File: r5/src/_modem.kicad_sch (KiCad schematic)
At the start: 54 parts, among them J1 , J12 U_FL-R-SMT-1_10_, J13 JAE_SIM_Card_SF72S006, J17 DNP, J2 , J3 , J4 , J5 , J6 , J7 , J8 , J9 , Q11 NX3008NBKW, Q5 NX3008NBKW, Q6 NX3008NBKW, Q7 NX3008NBKW, Q8 NX3008NBKW, Q9 NX3008NBKW, T10 , T11 , T8 , T9 , U7 Sierra_Wireless_RC7620, U8 ESD7004

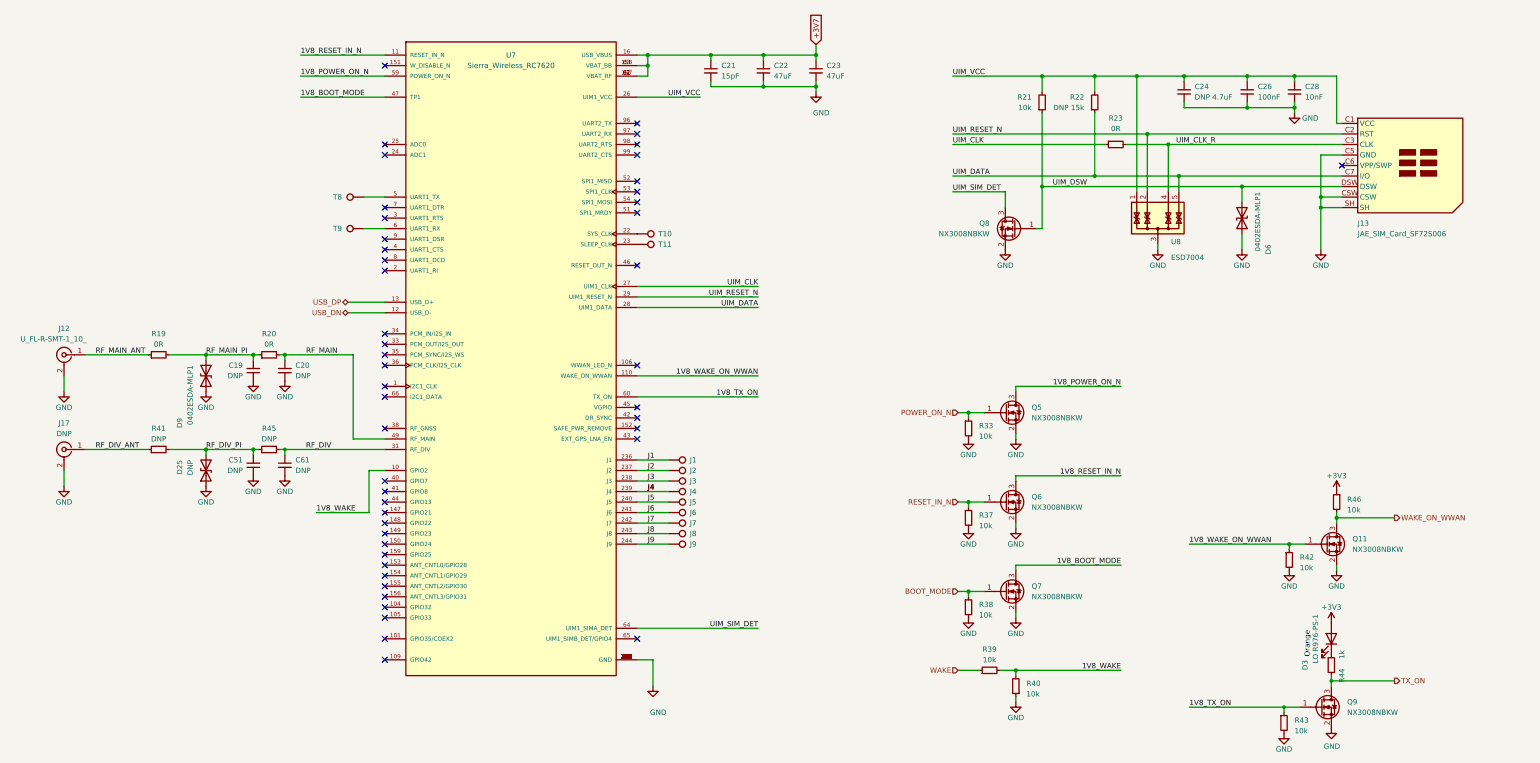
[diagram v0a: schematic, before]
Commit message: Updates to +/-15V supply. Additional output capacitance. Change to smaller inductor packages. Add 0R links to permit isolation of output. Mods to compensation network. Set feedback resistors to datasheet values.
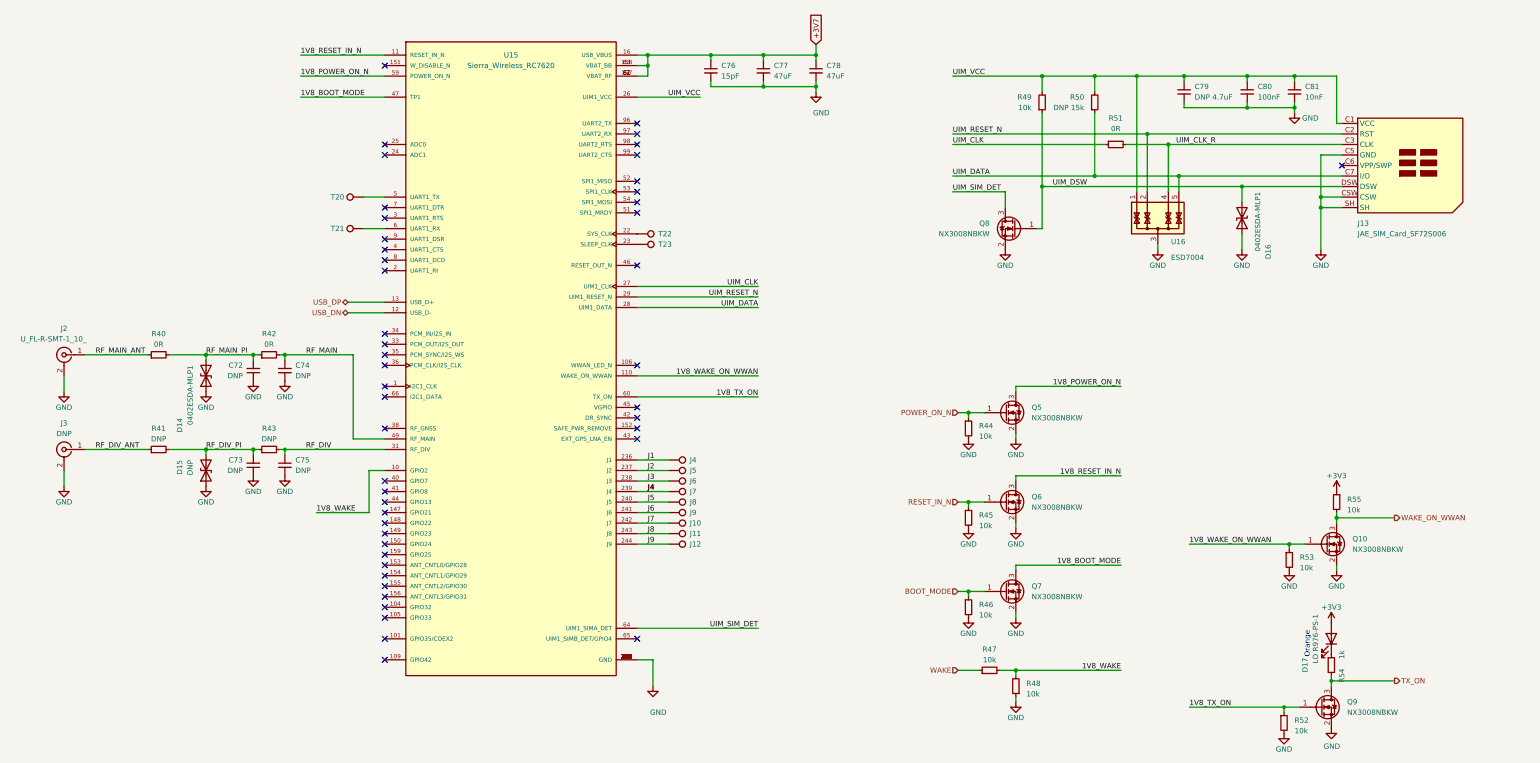
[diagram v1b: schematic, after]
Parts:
- renumbered C19 to C72, C51 to C73, C20 to C74, C61 to C75, C21 to C76, C22 to C77, C23 to C78, C24 to C79, C26 to C80, C28 to C81, D9 to D14, D25 to D15, D6 to D16, D3 to D17, J7 to J10, J8 to J11, J9 to J12, J12 to J2, J17 to J3, J1 to J4, J2 to J5, J3 to J6, J4 to J7, J5 to J8, J6 to J9, Q11 to Q10, R19 to R40, R20 to R42, R45 to R43, R33 to R44, R37 to R45, R38 to R46, R39 to R47, R40 to R48, R21 to R49, R22 to R50, R23 to R51, R43 to R52, R42 to R53, R44 to R54, R46 to R55, T8 to T20, T9 to T21, T10 to T22, T11 to T23, U7 to U15, U8 to U16

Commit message: Fix broken component annotation by importing back from PCB and fixing duplicates.
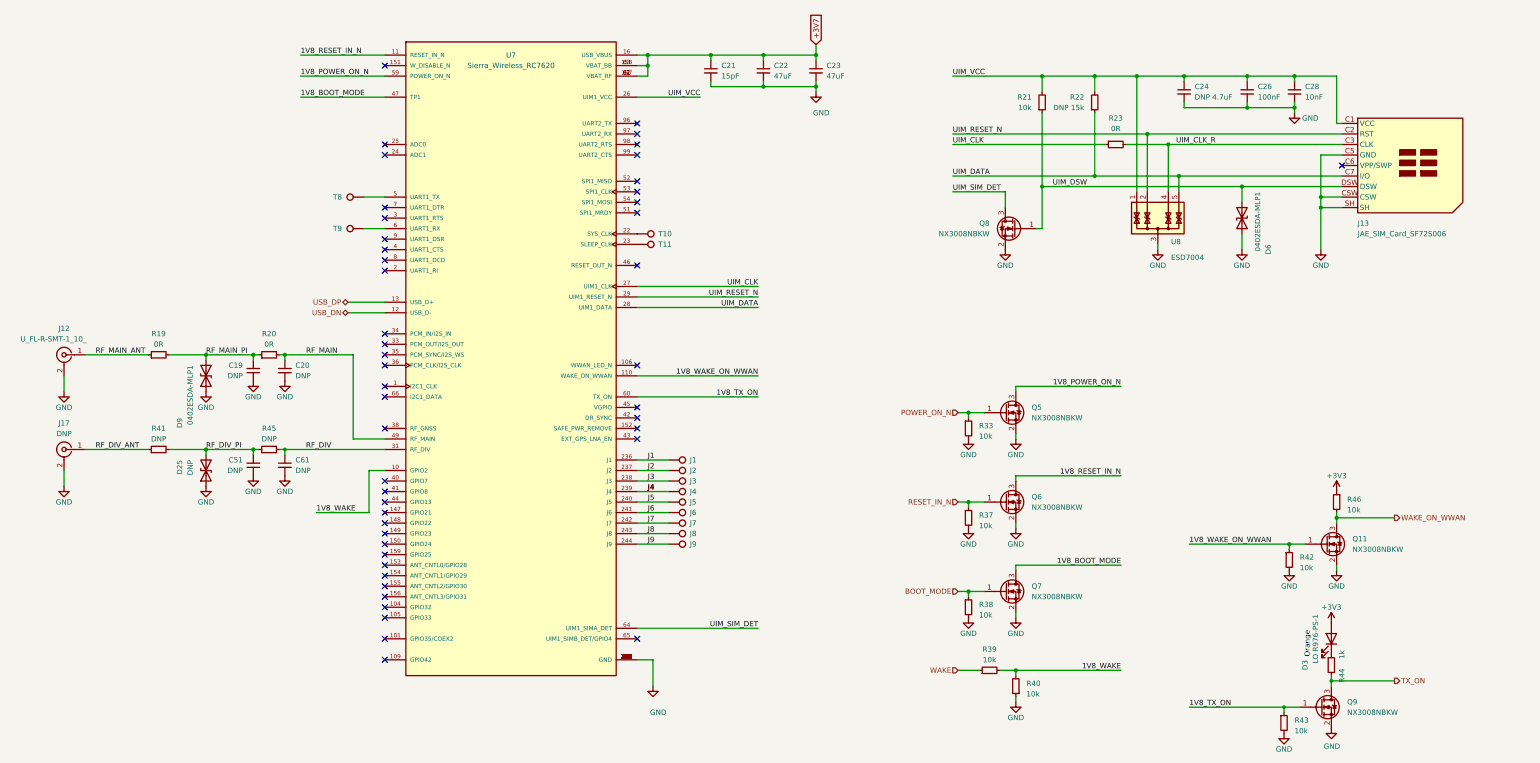
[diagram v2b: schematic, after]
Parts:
- renumbered C72 to C19, C74 to C20, C76 to C21, C77 to C22, C78 to C23, C79 to C24, C80 to C26, C81 to C28, C73 to C51, C75 to C61, D15 to D25, D17 to D3, D16 to D6, D14 to D9, J4 to J1, J2 to J12, J3 to J17, J5 to J2, J6 to J3, J7 to J4, J8 to J5, J9 to J6, J10 to J7, J11 to J8, J12 to J9, Q10 to Q11, R40 to R19, R42 to R20, R49 to R21, R50 to R22, R51 to R23, R44 to R33, R45 to R37, R46 to R38, R47 to R39, R48 to R40, R53 to R42, R52 to R43, R54 to R44, R43 to R45, R55 to R46, T22 to T10, T23 to T11, T20 to T8, T21 to T9, U15 to U7, U16 to U8

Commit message: Add testpoints to SIM bus
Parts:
- added T1 (x5): (no value), TestPoint:TestPoint_Pad_D1.0mm, symbol Connector:TestPoint
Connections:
- net UIM_CLK_R: now also T1.1
- net UIM_DATA: now also T1.1
- net UIM_DSW: now also T1.1
- net UIM_RESET_N: now also T1.1
- net UIM_VCC: now also T1.1
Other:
- moved on the sheet: J13

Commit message: Update layout to standardise on 0402 passives everywhere possible. This reduces the number of BoM lines. DRC passed. Add DRC exclusions for unavoidable violations
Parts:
- C21: footprint Capacitor_SMD:C_0603_1608Metric -> Capacitor_SMD:C_0402_1005Metric
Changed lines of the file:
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@@
       (effects (font (size 1.27 1.27)) (justify left))
     )
-    (property "Footprint" "Capacitor_SMD:C_0603_1608Metric" (at 187.96 64.77 0)
+    (property "Footprint" "Capacitor_SMD:C_0402_1005Metric" (at 187.96 64.77 0)
       (effects (font (size 1.27 1.27)) hide)
     )

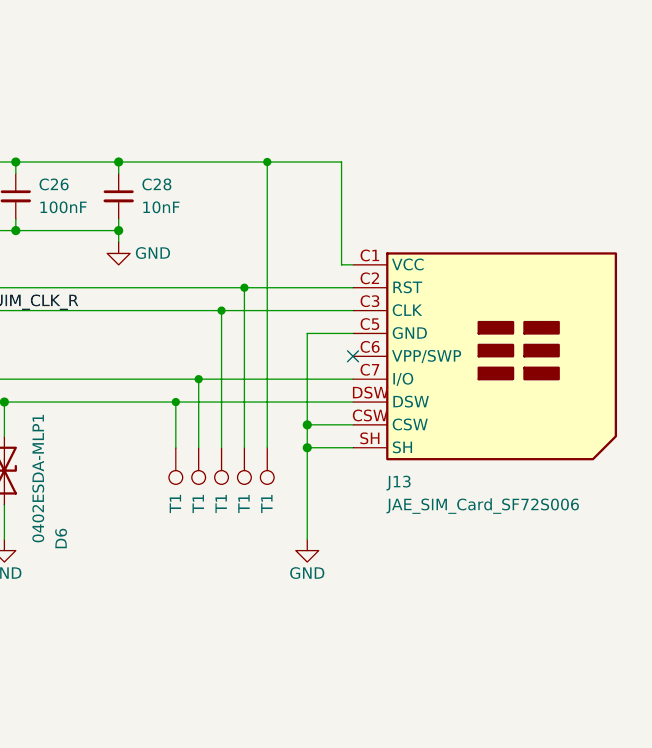
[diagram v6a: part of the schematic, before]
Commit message: Just realised I forgot to run the ERC. Added various PWR_FLAGs, corrected off-grid parts, etc. Updated board - no electrical changes.
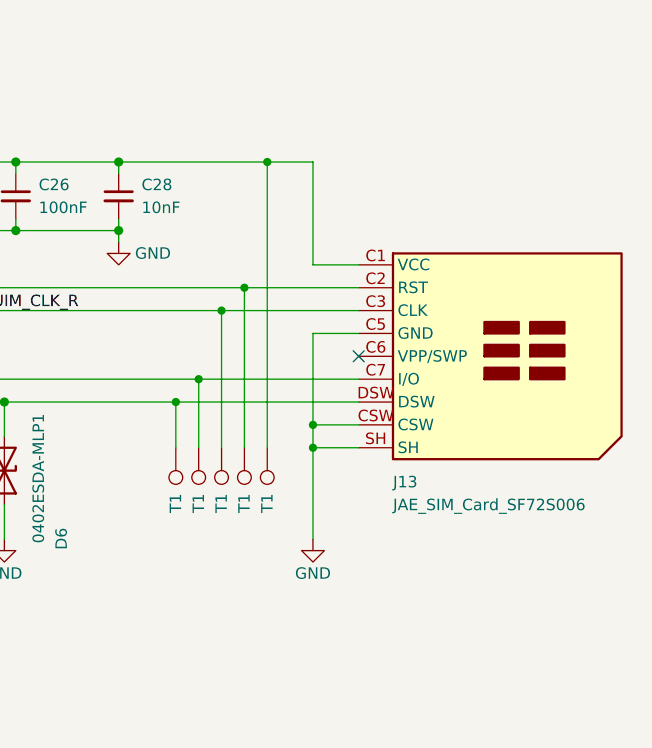
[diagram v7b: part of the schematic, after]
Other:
- moved on the sheet: J13
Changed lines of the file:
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@@
   (junction (at 77.47 156.21) (diameter 1.016) (color 0 0 0 0)
   )
-  (junction (at 349.885 95.25) (diameter 1.016) (color 0 0 0 0)
-  )
   (junction (at 317.5 66.04) (diameter 1.016) (color 0 0 0 0)
   )
@@
   (junction (at 66.04 156.21) (diameter 1.016) (color 0 0 0 0)
   )
+  (junction (at 350.52 97.79) (diameter 0) (color 0 0 0 0)
+  )
   (junction (at 337.82 212.09) (diameter 0) (color 0 0 0 0)
   )
@@
   (junction (at 280.67 90.17) (diameter 1.016) (color 0 0 0 0)
   )
-  (junction (at 349.885 97.79) (diameter 1.016) (color 0 0 0 0)
+  (junction (at 350.52 95.25) (diameter 0) (color 0 0 0 0)
   )
   (junction (at 200.66 60.96) (diameter 1.016) (color 0 0 0 0)
@@
   (no_connect (at 109.22 143.51))
   (no_connect (at 170.18 151.13))
-  (no_connect (at 354.965 87.63))
+  (no_connect (at 355.6 87.63))
   (wire (pts (xy 300.99 90.17) (xy 300.99 93.98))
     (stroke (width 0) (type solid))
@@
     (stroke (width 0) (type solid))
   )
-  (wire (pts (xy 353.695 66.04) (xy 345.44 66.04))
-    (stroke (width 0) (type solid))
-  )
-  (wire (pts (xy 353.695 77.47) (xy 353.695 66.04))
-    (stroke (width 0) (type solid))
-  )
-  (wire (pts (xy 354.965 77.47) (xy 353.695 77.47))
-    (stroke (width 0) (type solid))
-  )
-  (wire (pts (xy 342.9 80.01) (xy 354.965 80.01))
+  (wire (pts (xy 350.52 66.04) (xy 345.44 66.04))
+    (stroke (width 0) (type solid))
+  )
+  (wire (pts (xy 350.52 77.47) (xy 350.52 66.04))
+    (stroke (width 0) (type solid))
+  )
+  (wire (pts (xy 355.6 77.47) (xy 350.52 77.47))
+    (stroke (width 0) (type solid))
+  )
+  (wire (pts (xy 342.9 80.01) (xy 355.6 80.01))
     (stroke (width 0) (type solid))
   )
@@
     (stroke (width 0) (type solid))
   )
-  (wire (pts (xy 349.885 85.09) (xy 349.885 95.25))
-    (stroke (width 0) (type solid))
-  )
-  (wire (pts (xy 354.965 85.09) (xy 349.885 85.09))
+  (wire (pts (xy 350.52 85.09) (xy 350.52 95.25))
+    (stroke (width 0) (type solid))
+  )
+  (wire (pts (xy 355.6 85.09) (xy 350.52 85.09))
     (stroke (width 0) (type solid))
   )
@@
     (stroke (width 0) (type default))
   )
-  (wire (pts (xy 349.885 95.25) (xy 349.885 97.79))
-    (stroke (width 0) (type solid))
-  )
-  (wire (pts (xy 354.965 95.25) (xy 349.885 95.25))
-    (stroke (width 0) (type solid))
-  )
-  (wire (pts (xy 349.885 97.79) (xy 349.885 107.95))
-    (stroke (width 0) (type solid))
-  )
-  (wire (pts (xy 354.965 97.79) (xy 349.885 97.79))
+  (wire (pts (xy 350.52 95.25) (xy 350.52 97.79))
+    (stroke (width 0) (type solid))
+  )
+  (wire (pts (xy 355.6 95.25) (xy 350.52 95.25))
+    (stroke (width 0) (type solid))
+  )
+  (wire (pts (xy 350.52 97.79) (xy 350.52 107.95))
+    (stroke (width 0) (type solid))
+  )
+  (wire (pts (xy 355.6 97.79) (xy 350.52 97.79))
     (stroke (width 0) (type solid))
   )
@@
     (stroke (width 0) (type default))
   )
-  (wire (pts (xy 337.82 90.17) (xy 354.965 90.17))
+  (wire (pts (xy 337.82 90.17) (xy 355.6 90.17))
     (stroke (width 0) (type solid))
   )
@@
     (stroke (width 0) (type default))
   )
-  (wire (pts (xy 335.28 92.71) (xy 354.965 92.71))
+  (wire (pts (xy 335.28 92.71) (xy 355.6 92.71))
     (stroke (width 0) (type solid))
   )
@@
     (stroke (width 0) (type solid))
   )
-  (wire (pts (xy 340.36 82.55) (xy 354.965 82.55))
+  (wire (pts (xy 340.36 82.55) (xy 355.6 82.55))
     (stroke (width 0) (type solid))
   )
@@
     )
   )
-  (symbol (lib_id "power:GND") (at 349.885 107.95 0) (unit 1)
-    (exclude_from_sim no) (in_bom yes) (on_board yes) (dnp no)
-    (property "Reference" "#PWR0152" (at 349.885 114.3 0)
-      (effects (font (size 1.27 1.27)) hide)
-    )
-    (property "Value" "GND" (at 349.885 111.76 0)
-      (effects (font (size 1.27 1.27)))
-    )
-    (property "Footprint" "" (at 349.885 107.95 0)
-      (effects (font (size 1.27 1.27)) hide)
-    )
-    (property "Datasheet" "" (at 349.885 107.95 0)
-      (effects (font (size 1.27 1.27)) hide)
-    )
-    (property "Description" "" (at 349.885 107.95 0)
+  (symbol (lib_id "power:GND") (at 350.52 107.95 0) (unit 1)
+    (exclude_from_sim no) (in_bom yes) (on_board yes) (dnp no)
+    (property "Reference" "#PWR0152" (at 350.52 114.3 0)
+      (effects (font (size 1.27 1.27)) hide)
+    )
+    (property "Value" "GND" (at 350.52 111.76 0)
+      (effects (font (size 1.27 1.27)))
+    )
+    (property "Footprint" "" (at 350.52 107.95 0)
+      (effects (font (size 1.27 1.27)) hide)
+    )
+    (property "Datasheet" "" (at 350.52 107.95 0)
+      (effects (font (size 1.27 1.27)) hide)
+    )
+    (property "Description" "" (at 350.52 107.95 0)
       (effects (font (size 1.27 1.27)) hide)
     )
@@
     )
   )
-  (symbol (lib_id "Connector:JAE_SIM_Card_SF72S006") (at 354.965 87.63 0) (unit 1)
-    (exclude_from_sim no) (in_bom yes) (on_board yes) (dnp no)
-    (property "Reference" "J13" (at 358.775 101.6 0)
-      (effects (font (size 1.27 1.27)) (justify left))
-    )
-    (property "Value" "JAE_SIM_Card_SF72S006" (at 358.775 104.14 0)
-      (effects (font (size 1.27 1.27)) (justify left))
-    )
-    (property "Footprint" "Connector_JAE:JAE_SIM_Card_SF72S006" (at 366.395 101.6 0)
-      (effects (font (size 1.27 1.27)) hide)
-    )
-    (property "Datasheet" "https://www.jae.com/direct/topics/topics_file_download/topics_id=68892&ext_no=06&index=0&_lang=en&v=202003111511468456809" (at 368.935 87.63 0)
-      (effects (font (size 1.27 1.27)) hide)
-    )
-    (property "Description" "" (at 354.965 87.63 0)
-      (effects (font (size 1.27 1.27)) hide)
-    )
+  (symbol (lib_id "Connector:JAE_SIM_Card_SF72S006") (at 355.6 87.63 0) (unit 1)
+    (exclude_from_sim no) (in_bom yes) (on_board yes) (dnp no)
+    (property "Reference" "J13" (at 359.41 101.6 0)
+      (effects (font (size 1.27 1.27)) (justify left))
+    )
+    (property "Value" "JAE_SIM_Card_SF72S006" (at 359.41 104.14 0)
+      (effects (font (size 1.27 1.27)) (justify left))
+    )
+    (property "Footprint" "Connector_JAE:JAE_SIM_Card_SF72S006" (at 367.03 101.6 0)
+      (effects (font (size 1.27 1.27)) hide)
+    )
+    (property "Datasheet" "https://www.jae.com/direct/topics/topics_file_download/topics_id=68892&ext_no=06&index=0&_lang=en&v=202003111511468456809" (at 369.57 87.63 0)
+      (effects (font (size 1.27 1.27)) hide)
+    )
+    (property "Description" "" (at 355.6 87.63 0)
+      (effects (font (size 1.27 1.27)) hide)
+    )

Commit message: Bring one random DNP 4.7uF 0805 into parity with the rest of the board that uses 0603 (except the high voltage ones which are 1206)
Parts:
- C24: footprint Capacitor_SMD:C_0805_2012Metric -> Capacitor_SMD:C_0603_1608Metric
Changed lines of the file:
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@@
       (effects (font (size 1.27 1.27)) (justify left))
     )
-    (property "Footprint" "Capacitor_SMD:C_0805_2012Metric" (at 302.26 69.85 0)
+    (property "Footprint" "Capacitor_SMD:C_0603_1608Metric" (at 302.26 69.85 0)
       (effects (font (size 1.27 1.27)) hide)
     )
